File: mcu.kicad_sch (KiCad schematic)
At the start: 21 parts, among them U1 STM32F723VET6, U2 USBLC6-2SC6

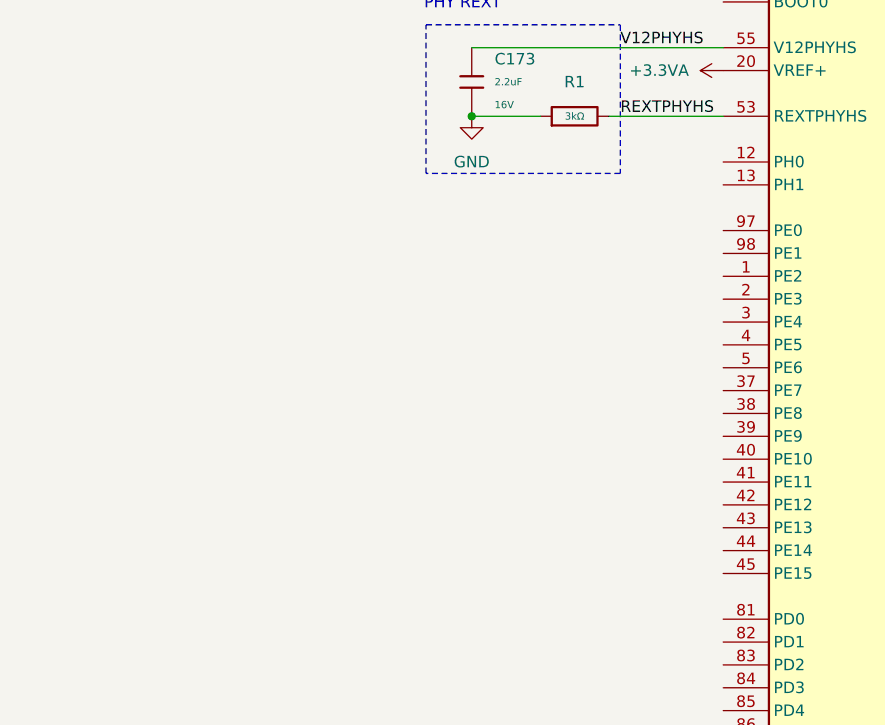
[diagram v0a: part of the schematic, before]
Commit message: add capacitor to mux vcc
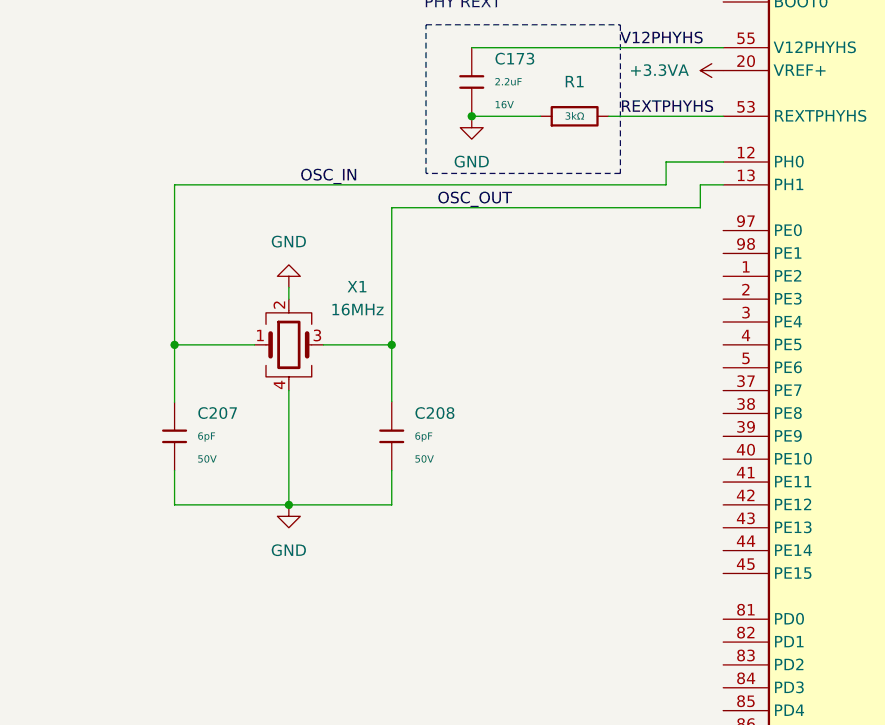
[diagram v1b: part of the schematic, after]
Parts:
- added C207, C208: 6pF, PCM_JLCPCB:C_0603, symbol PCM_JLCPCB-Capacitors:0603,6pF
- added X1: 16MHz, Crystal:Crystal_SMD_2520-4Pin_2.5x2.0mm, symbol Device:Crystal_GND24
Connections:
- net GND: now also C207.2, C208.2, X1.2, X1.4
- net OSC_IN: now reaches U1.12 (PH0)
- net OSC_IN: now also C207.1, X1.1
- net OSC_OUT: now reaches U1.13 (PH1)
- net OSC_OUT: now also C208.1, X1.3

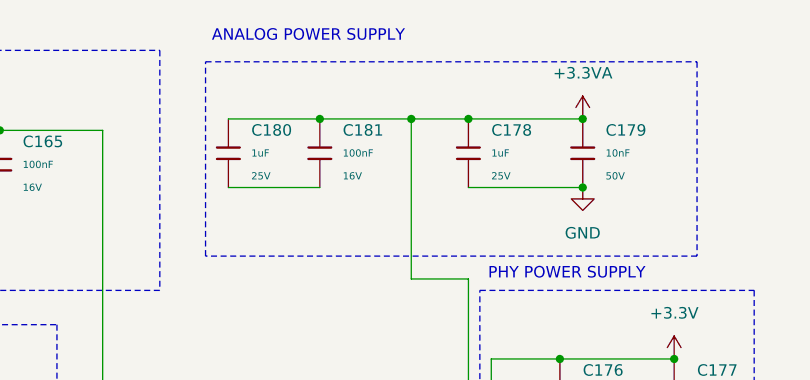
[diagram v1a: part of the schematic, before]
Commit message: start placing mcu capacitor
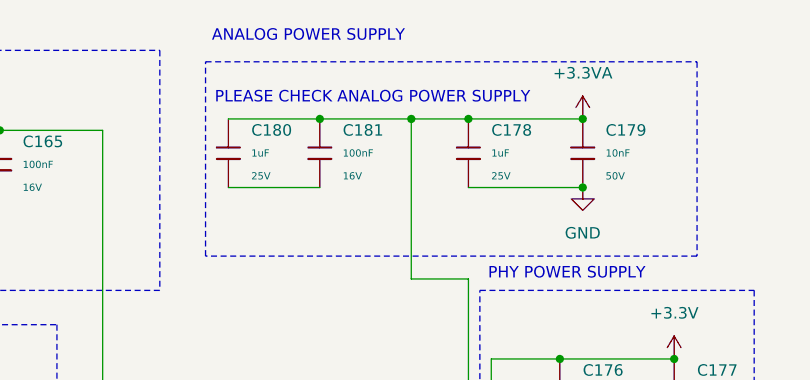
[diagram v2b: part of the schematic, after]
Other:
- note added: "PLEASE CHECK ANALOG POWER SUPPLY"
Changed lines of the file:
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@@
+		)
+	)
+	(text "PLEASE CHECK ANALOG POWER SUPPLY"
+		(exclude_from_sim no)
+		(at 180.086 21.844 0)
+		(effects
+			(font
+				(size 1.27 1.27)
+			)
+			(justify left)
 		)
 	)

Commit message: start usb
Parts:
- added C214: 100nF, PCM_JLCPCB:C_0402, symbol PCM_JLCPCB-Capacitors:0402,100nF
- added J201: Connector, USB-TYPE-C-16P, Connector_USB:USB_C_Receptacle_XKB_U262-16XN-4BVC11, symbol PCM_JLCPCB-Extended:Connector, USB-TYPE-C-16P
- added R201, R202: 5.1kΩ, PCM_JLCPCB:R_0402, symbol PCM_JLCPCB-Resistors:0402,5.1kΩ
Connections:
- net GND: now also U2.2 (GND), C214.2, J201.A12B1 (GND), J201.B12A1 (GND), J201.S1 (SHIELD), R201.1, R202.1
- net USB_PLUG_D-: now reaches U2.1 (I/O1)
- net USB_PLUG_D-: now also J201.A7 (D-), J201.B7 (D-)
- net USB_PLUG_D+: now reaches U2.3 (I/O2)
- net USB_PLUG_D+: now also J201.A6 (D+), J201.B6 (D+)
- net USB_D+: now reaches U2.4 (I/O2)
- net VBUS: now reaches U2.5 (VBUS)
- net VBUS: now also C214.1, J201.A9B4 (VBUS), J201.B9A4 (VBUS)
- net USB_D-: now reaches U2.6 (I/O1)
- new net: J201.A5 (CC1), R201.2
- new net: J201.B5 (CC2), R202.2
- no-connect marks 0 -> 2
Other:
- note added: "ELECTROSTATIC DISCHARGE PROTECTION"
- note added: "HSE"
- note added: "TODO: ADD 3A FUZE"
- note added: "USB TYPE C CONNECTOR"
- moved on the sheet: U2

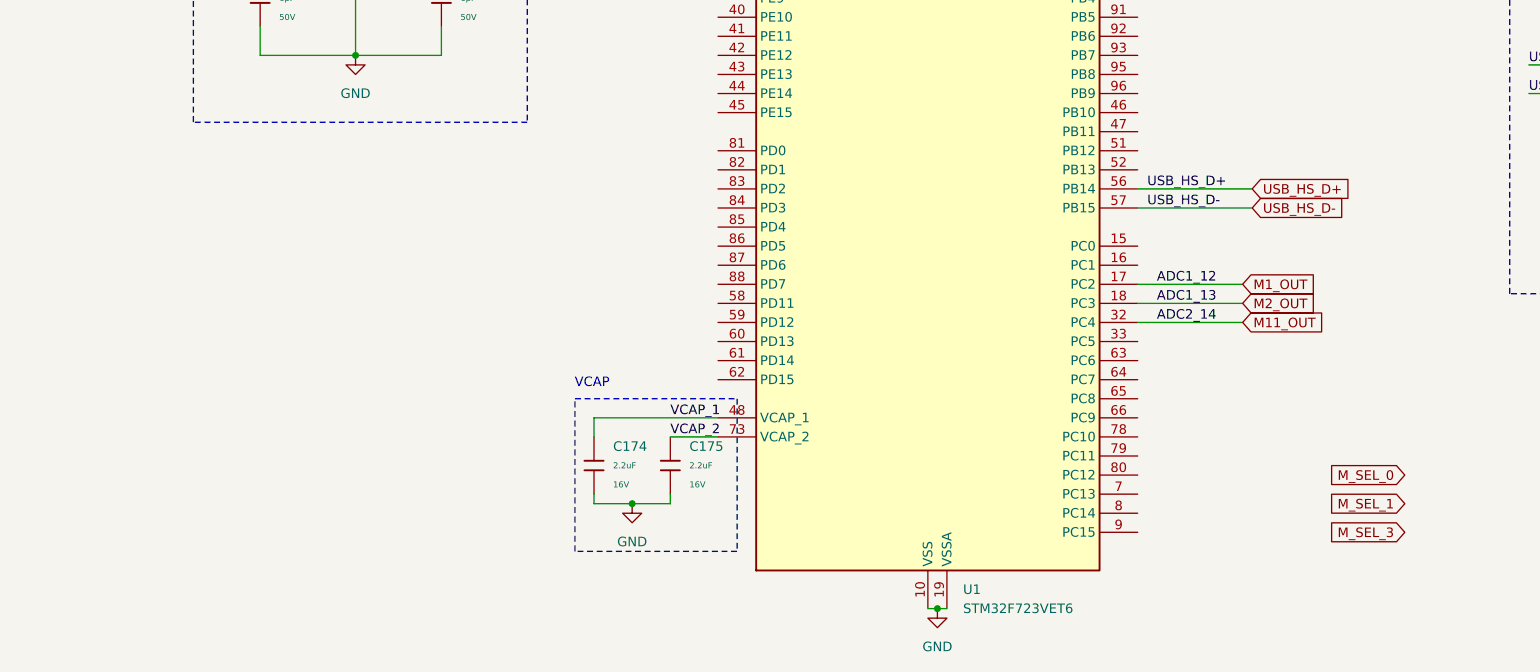
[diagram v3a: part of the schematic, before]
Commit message: start analog ldo layout
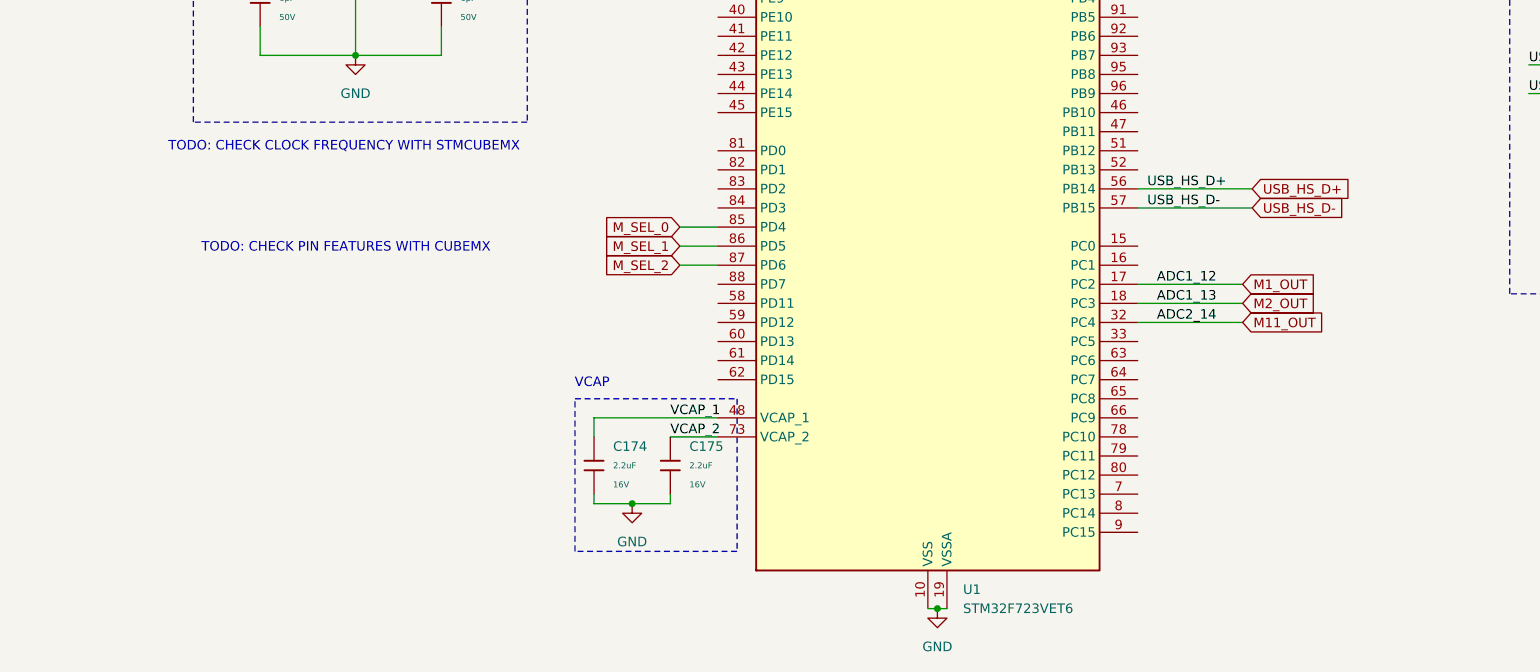
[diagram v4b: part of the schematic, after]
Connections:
- net M_SEL_0: now also U1.85 (PD4)
- net M_SEL_1: now also U1.86 (PD5)
- net M_SEL_2: now reaches U1.87 (PD6)
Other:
- note added: "TODO: CHECK CLOCK FREQUENCY WITH STMCUBEMX"
- note added: "TODO: CHECK PIN FEATURES WITH CUBEMX"
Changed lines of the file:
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@@
+		)
+	)
+	(text "TODO: CHECK CLOCK FREQUENCY WITH STMCUBEMX"
+		(exclude_from_sim no)
+		(at 122.936 150.622 0)
+		(effects
+			(font
+				(size 1.27 1.27)
+			)
 		)
 	)
@@
 		)
 	)
+	(text "TODO: CHECK PIN FEATURES WITH CUBEMX"
+		(exclude_from_sim no)
+		(at 123.19 164.084 0)
+		(effects
+			(font
+				(size 1.27 1.27)
+			)
+		)
+	)
 	(junction
 		(at 161.29 198.12)
@@
 	(wire
 		(pts
+			(xy 167.64 163.83) (xy 172.72 163.83)
+		)
+		(stroke
+			(width 0)
+			(type default)
+		)
+	)
+	(wire
+		(pts
 			(xy 181.61 24.13) (xy 191.77 24.13)
 		)
@@
 	(wire
 		(pts
+			(xy 167.64 166.37) (xy 172.72 166.37)
+		)
+		(stroke
+			(width 0)
+			(type default)
+		)
+	)
+	(wire
+		(pts
 			(xy 167.64 25.4) (xy 167.64 67.31)
 		)
@@
 		(pts
 			(xy 200.66 67.31) (xy 203.2 67.31)
+		)
+		(stroke
+			(width 0)
+			(type default)
+		)
+	)
+	(wire
+		(pts
+			(xy 167.64 161.29) (xy 172.72 161.29)
 		)
 		(stroke
@@
 			)
 			(justify left bottom)
-		)
-	)
-	(global_label "M_SEL_3"
-		(shape input)
-		(at 264.16 201.93 180)
-		(fields_autoplaced yes)
-		(effects
-			(font
-				(size 1.27 1.27)
-			)
-			(justify right)
-		)
-		(property "Intersheetrefs" "${INTERSHEET_REFS}"
-			(at 253.1921 201.93 0)
-			(effects
-				(font
-					(size 1.27 1.27)
-				)
-				(justify right)
-				(hide yes)
-			)
 		)
 	)
@@
 	(global_label "M_SEL_1"
 		(shape input)
-		(at 264.16 198.12 180)
+		(at 167.64 163.83 180)
 		(fields_autoplaced yes)
 		(effects
@@
 		)
 		(property "Intersheetrefs" "${INTERSHEET_REFS}"
-			(at 253.1921 198.12 0)
+			(at 156.6721 163.83 0)
+			(effects
+				(font
+					(size 1.27 1.27)
+				)
+				(justify right)
+				(hide yes)
+			)
+		)
+	)
+	(global_label "M_SEL_0"
+		(shape input)
+		(at 167.64 161.29 180)
+		(fields_autoplaced yes)
+		(effects
+			(font
+				(size 1.27 1.27)
+			)
+			(justify right)
+		)
+		(property "Intersheetrefs" "${INTERSHEET_REFS}"
+			(at 156.6721 161.29 0)
+			(effects
+				(font
+					(size 1.27 1.27)
+				)
+				(justify right)
+				(hide yes)
+			)
+		)
+	)
+	(global_label "M_SEL_2"
+		(shape input)
+		(at 167.64 166.37 180)
+		(fields_autoplaced yes)
+		(effects
+			(font
+				(size 1.27 1.27)
+			)
+			(justify right)
+		)
+		(property "Intersheetrefs" "${INTERSHEET_REFS}"
+			(at 156.6721 166.37 0)
 			(effects
 				(font
@@
 				(hide yes)
 			)
-		)
-	)
-	(global_label "M_SEL_0"
-		(shape input)
-		(at 264.16 194.31 180)
-		(fields_autoplaced yes)
-		(effects
-			(font
-				(size 1.27 1.27)
-			)
-			(justify right)
-		)
-		(property "Intersheetrefs" "${INTERSHEET_REFS}"
-			(at 253.1921 194.31 0)
-			(effects
-				(font
-					(size 1.27 1.27)
-				)
-				(justify right)
-				(hide yes)
-			)

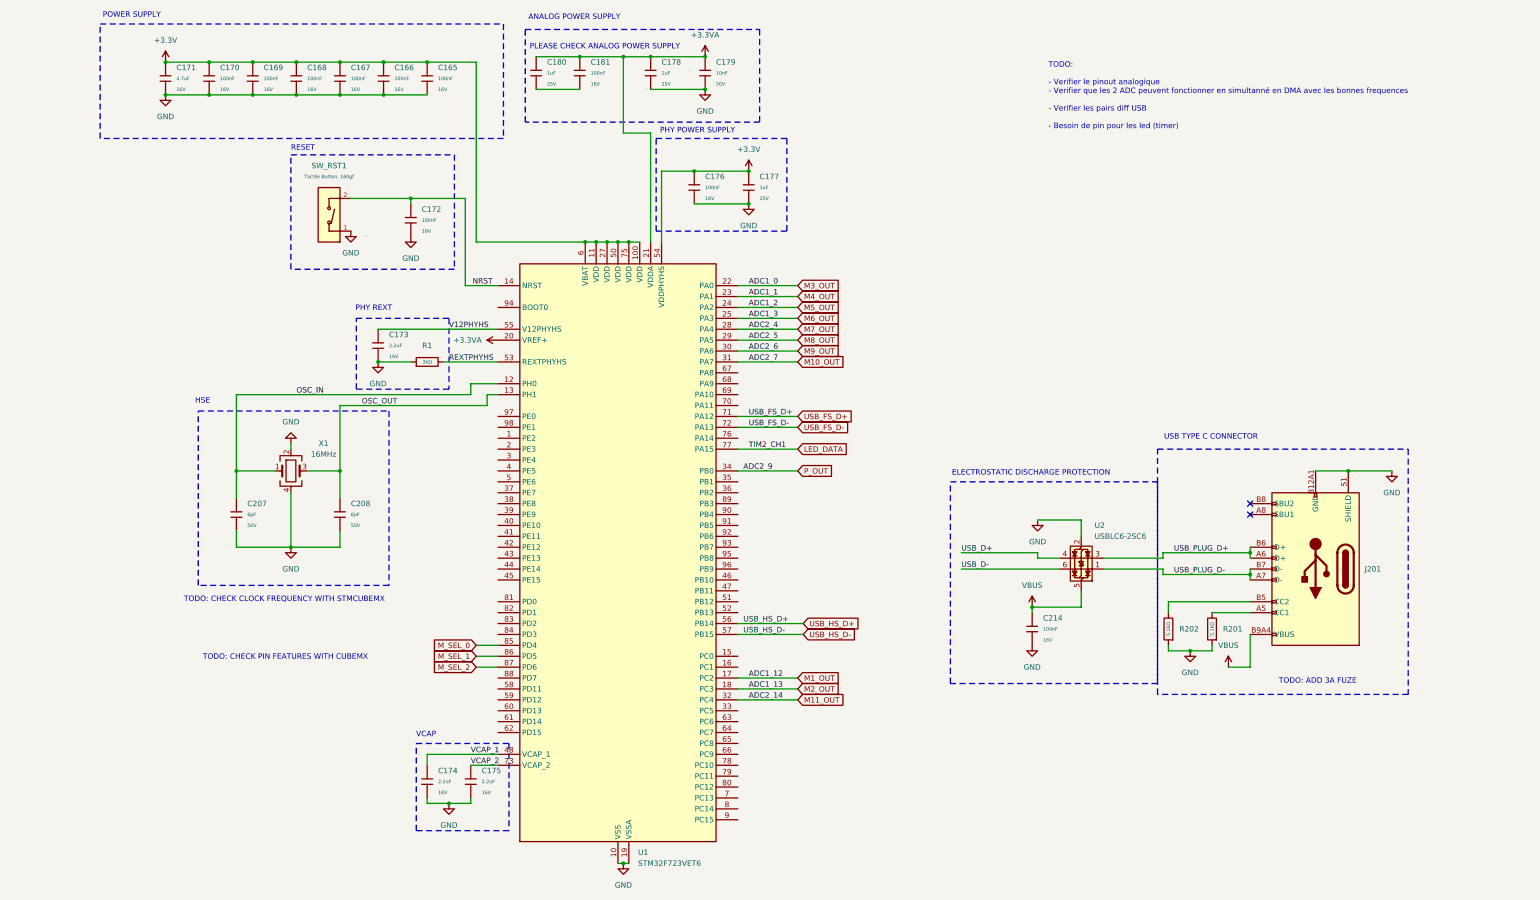
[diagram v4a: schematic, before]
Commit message: fix usb data line and add dfu and mux usb
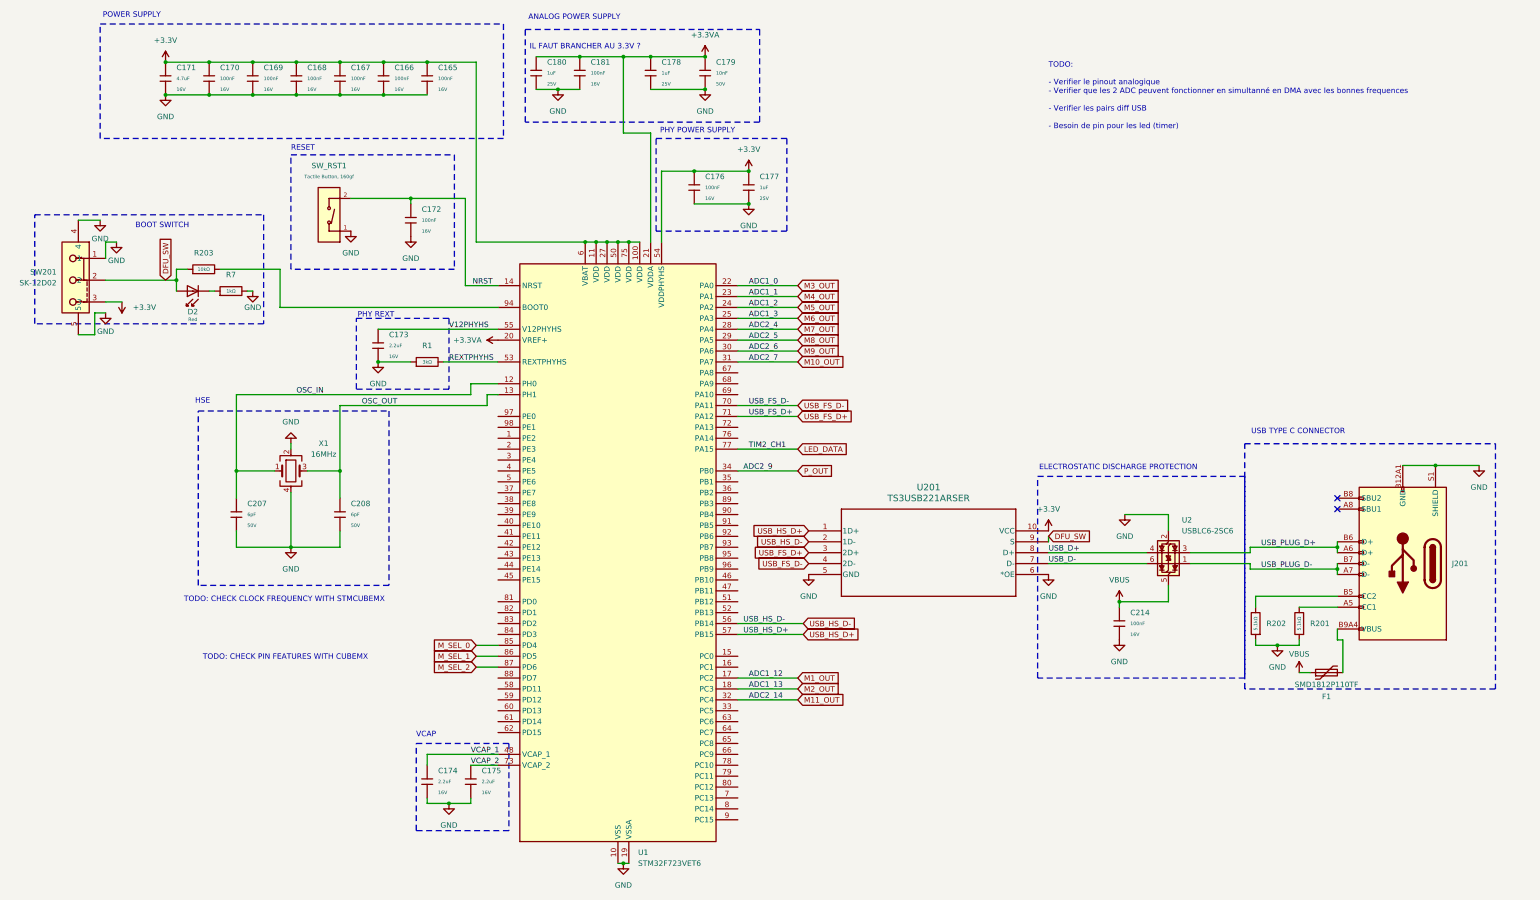
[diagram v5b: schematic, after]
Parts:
- added D2: Red, PCM_JLCPCB:D_0603, symbol PCM_JLCPCB-Diodes:LED,0603,Red
- added F1: SMD1812P110TF, Fuse:Fuse_1812_4532Metric, symbol Device:Polyfuse
- added R203: 10kΩ, PCM_JLCPCB:R_0402, symbol PCM_JLCPCB-Resistors:0402,10kΩ
- added R7: 1kΩ, PCM_JLCPCB:R_0402, symbol PCM_JLCPCB-Resistors:0402,1kΩ
- added SW201: SK-12D02, easyeda2kicad:SW-TH_SK-12D02VG3, symbol easyeda2kicad:SK-12D02
- added U201: TS3USB221ARSER, footprints:RSE10, symbol 2025-12-06_14-23-22:TS3USB221ARSER
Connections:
- net +3.3V: now also SW201.3, U201.10 (VCC)
- net GND: now also C180.2, C181.2, R7.2, SW201.1, SW201.4, SW201.5, U201.5 (GND), U201.6 (*OE)
- net USB_D+: now also U201.8 (D+)
- net USB_D-: now also U201.7 (D-)
- net USB_FS_D+: now also U201.3 (2D+)
- net USB_FS_D-: now also U1.70 (PA11), U201.4 (2D-); no longer U1.72 (PA13)
- net USB_HS_D+: now also U1.57 (PB15), U201.1 (1D+); no longer U1.56 (PB14)
- net USB_HS_D-: now also U1.56 (PB14), U201.2 (1D-); no longer U1.57 (PB15)
- net VBUS: now also F1.1; no longer J201.A9B4 (VBUS), J201.B9A4 (VBUS)
- net at U1.94 (BOOT0): now also R203.2
- new net: D2.1, R7.1
- new net: F1.2, J201.A9B4 (VBUS), J201.B9A4 (VBUS)
- new net DFU_SW: D2.2, R203.1, SW201.2, U201.9 (S)
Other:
- note added: "BOOT SWITCH"
- note added: "IL FAUT BRANCHER AU 3.3V ?"
- note removed: "PLEASE CHECK ANALOG POWER SUPPLY"
- note removed: "TODO: ADD 3A FUZE"
- moved on the sheet: C214, J201, R201, R202, U2
